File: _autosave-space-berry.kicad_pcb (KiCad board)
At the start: 6 copper layers, 97 parts, among them J1 ARJM11C7-502-AB-ER2-T, Q1 SiS415DNT, Q2 TSM2302CX, U11 RTL8211F-CG, U12 K4A8G165WC-BCTD, U13 XCZU15EG-2FFVB1156E, U6 TLV75801PDBV, U7 TLV75801PDBV, U8 TLV75801PDBV, U9 TLV75801PDBV

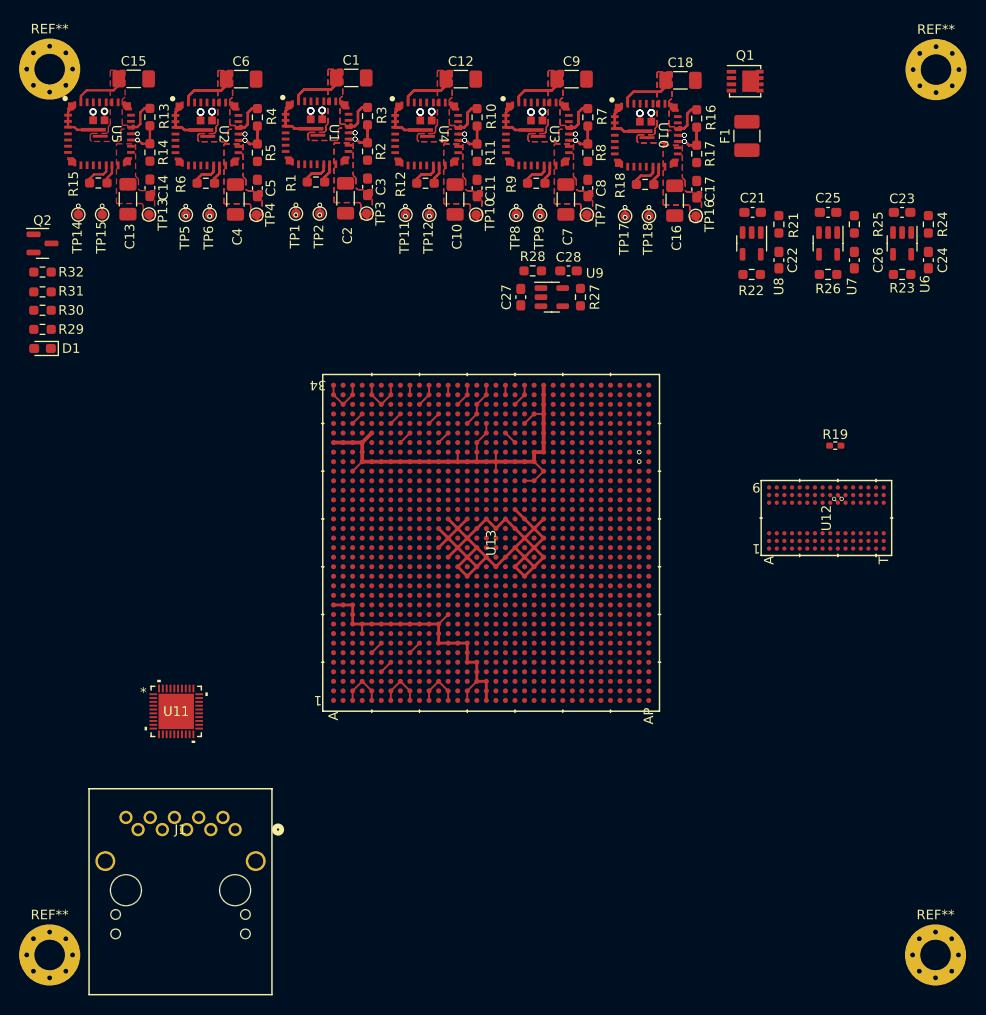
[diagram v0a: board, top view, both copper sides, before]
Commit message: DDR4 added
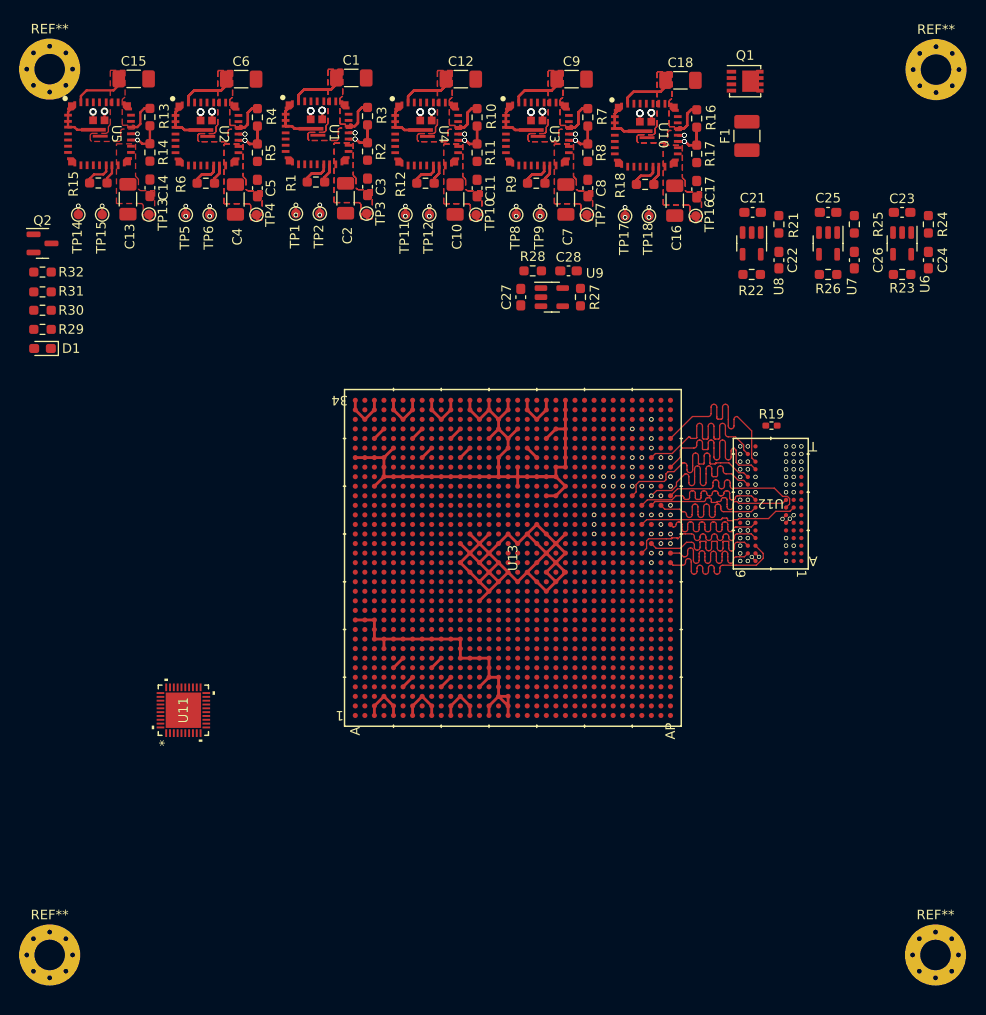
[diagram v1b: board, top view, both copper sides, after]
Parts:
- removed J1: ARJM11C7-502-AB-ER2-T, lib:ARJM11C7-502-AB-ER2-T_ABR
- moved R19 7.00 mm to (138.3, 69.1), turned to 180 degrees
- moved U12 6.02 mm to (138.2, 77.2), turned to 180 degrees
- moved U13 2.77 mm to (111.2, 82.9)
- moved U11 0.76 mm to (76.8, 98.9), turned to 90 degrees
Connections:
- U11 pad 1: unconnected-(U11A-MDIP0-Pad1) -> ETH_TR1+
- U11 pad 10: unconnected-(U11A-MDIN3-Pad10) -> ETH_TR4-
- U11 pad 15: unconnected-(U11A-TXD3-Pad15) -> ETH_TXD3
- U11 pad 16: unconnected-(U11A-TXD2-Pad16) -> ETH_TXD2
- U11 pad 17: unconnected-(U11A-TXD1-Pad17) -> ETH_TXD1
- U11 pad 18: unconnected-(U11A-TXD0-Pad18) -> ETH_TXD0
- U11 pad 2: unconnected-(U11A-MDIN0-Pad2) -> ETH_TR1-
- U11 pad 22: unconnected-(U11A-RXD3/PHYAD0-Pad22) -> Net-(U11A-RXD3/PHYAD0)
- U11 pad 23: unconnected-(U11A-RXD2/PLLOFF-Pad23) -> Net-(U11A-RXD2/PLLOFF)
- U11 pad 24: unconnected-(U11A-RXD1/TXDLY-Pad24) -> Net-(U11A-RXD1/TXDLY)
- U11 pad 25: unconnected-(U11A-RXD0/RXDLY-Pad25) -> Net-(U11A-RXD0/RXDLY)
- U11 pad 4: unconnected-(U11A-MDIP1-Pad4) -> ETH_TR2+
- U11 pad 5: unconnected-(U11A-MDIN1-Pad5) -> ETH_TR2-
- U11 pad 6: unconnected-(U11A-MDIP2-Pad6) -> ETH_TR3+
- U11 pad 7: unconnected-(U11A-MDIN2-Pad7) -> ETH_TR3-
- U11 pad 9: unconnected-(U11A-MDIP3-Pad9) -> ETH_TR4+
- U13 pad AL18: DDR_BY_L7 -> DDR_BY_U15
- U13 pad AL21: DDR_BY_U12 -> DDR_BY_L4
- U13 pad AL22: DDR_BY_U13 -> DDR_BY_L5
- U13 pad AL23: DDR_BY_U15 -> DDR_BY_L7
- U13 pad AM18: DDR_BY_L6 -> DDR_BY_U14
- U13 pad AM19: DDR_BY_L5 -> DDR_BY_U13
- U13 pad AM20: DDR_BY_L4 -> DDR_BY_U12
- U13 pad AM23: DDR_BY_U14 -> DDR_BY_L6
- U13 pad AN18: DDR_DQS0+ -> DDR_DQS1+
- U13 pad AN19: DDR_DQS0- -> DDR_DQS1-
- U13 pad AN21: DDR_DQS1+ -> DDR_DQS0+
- U13 pad AN22: DDR_DQS1- -> DDR_DQS0-
- U13 pad AN23: DDR_BY_U11 -> DDR_BY_L3
- U13 pad AP17: DDR_BY_L3 -> DDR_BY_U11
- U13 pad AP18: DDR_BY_L1 -> DDR_BY_U9
- U13 pad AP19: DDR_BY_L2 -> DDR_BY_U10
- U13 pad AP20: DDR_BY_L0 -> DDR_BY_U8
- U13 pad AP21: DDR_BY_U9 -> DDR_BY_L1
- U13 pad AP22: DDR_BY_U8 -> DDR_BY_L0
- U13 pad AP24: DDR_BY_U10 -> DDR_BY_L2
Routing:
- net DDR_PAR: track 0.00 -> 29.4 mm, vias 0 -> 2
- net DDR_RES: track 0.00 -> 26.9 mm, vias 0 -> 2
- net DDR_ODT: track 0.00 -> 21.9 mm, vias 0 -> 2
- net DDR_BG0: track 0.00 -> 21.8 mm, vias 0 -> 2
- net DDR_A15: track 0.00 -> 20.5 mm
- net DDR_A1: track 0.00 -> 20.5 mm
- net DDR_A7: track 0.00 -> 20.4 mm
- net DDR_BA0: track 0.00 -> 20.4 mm, vias 0 -> 2
- net DDR_A3: track 0.00 -> 20.4 mm
- net DDR_ALTER: track 0.00 -> 20.4 mm, vias 0 -> 2
- net DDR_A16: track 0.00 -> 20.4 mm, vias 0 -> 1
- net DDR_A5: track 0.00 -> 20.2 mm, vias 0 -> 2
- net DDR_A9: track 0.00 -> 20.1 mm, vias 0 -> 2
- net DDR_A12: track 0.00 -> 20.1 mm, vias 0 -> 2
- net DDR_A13: track 0.00 -> 20.1 mm, vias 0 -> 2
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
